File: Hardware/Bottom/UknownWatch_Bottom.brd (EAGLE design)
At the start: 33 x 33 mm, 31 parts, among them U1 AD5242-SO16

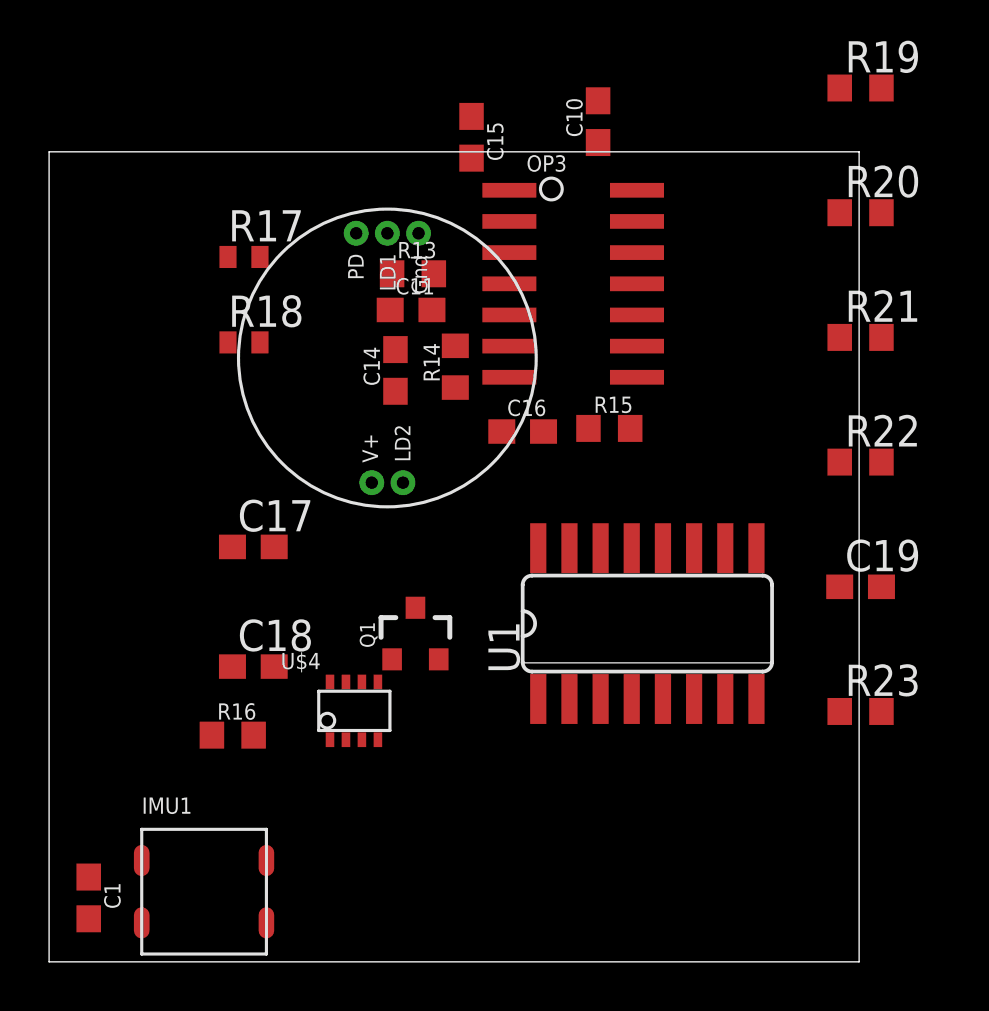
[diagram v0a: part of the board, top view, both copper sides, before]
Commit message: Added connections from bottom to top board and other various changes.
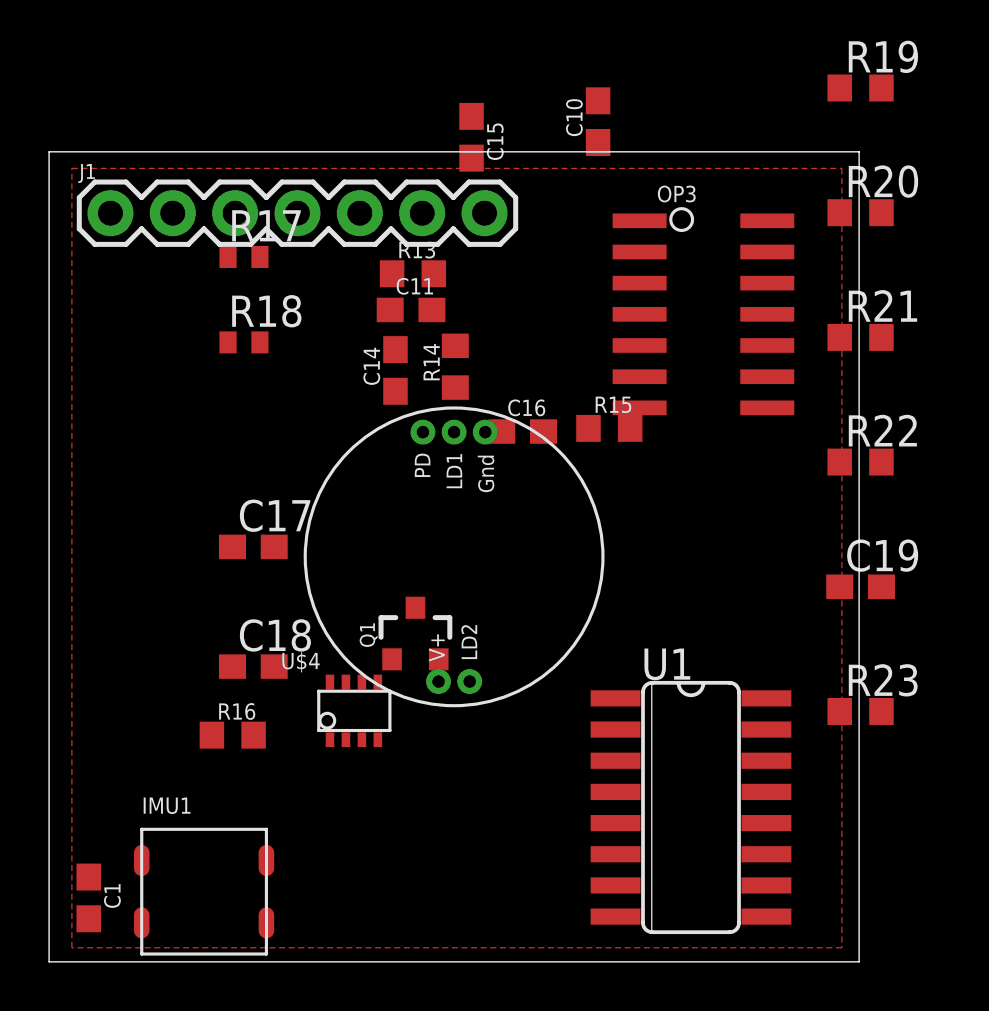
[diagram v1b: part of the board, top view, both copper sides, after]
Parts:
- added J1: (no value), LinnesLab-Connectors:1X07
- moved U$3 8.55 mm to (19.0, 19.0)
- moved U1 7.70 mm to (28.7, 8.79), turned to 270 degrees
- moved OP3 5.45 mm to (29.2, 28.9)
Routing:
- added copper zone on layer 1, net 3.3V

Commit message: Made all changes associated wih take 002
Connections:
- removed net LED.CTRL: U$4.8
- removed net TIA: C10.2, C15.1, OP4.1, U1.3
- new net A6/TIA: C10.2, C15.1, J1.5, OP4.1, U1.3
- new net A7/PPG: C21.2, J1.7, OP3.1
- new net D29/LED.CTRL: J1.6, U$4.8
- net PPG: no longer C21.2, OP3.1
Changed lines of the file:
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@@
 <wire x1="11.3538" y1="4.0894" x2="15.8946" y2="11.549" width="0" layer="19" extent="1-1"/>
 </signal>
-<signal name="TIA">
+<signal name="A6/TIA">
 <contactref element="C10" pad="2"/>
 <contactref element="U1" pad="3"/>
 <contactref element="C15" pad="1"/>
 <contactref element="OP4" pad="1"/>
+<contactref element="J1" pad="5"/>
 <wire x1="24.8666" y1="37.5784" x2="43.5" y2="31.714" width="0" layer="19" extent="1-1"/>
 <wire x1="19.7104" y1="36.9434" x2="24.8666" y2="37.5784" width="0" layer="19" extent="1-1"/>
-<wire x1="25.5778" y1="10.6934" x2="24.8666" y2="37.5784" width="0" layer="19" extent="1-1"/>
+<wire x1="15.16" y1="33" x2="19.7104" y2="36.9434" width="0" layer="19" extent="1-1"/>
+<wire x1="25.5778" y1="10.6934" x2="15.16" y2="33" width="0" layer="19" extent="1-1"/>
 </signal>
 <signal name="PD.C">
@@
 <wire x1="9.1322" y1="11.7348" x2="13.9446" y2="11.549" width="0" layer="19" extent="1-1"/>
 </signal>
-<signal name="LED.CTRL">
+<signal name="D29/LED.CTRL">
 <contactref element="U$4" pad="8"/>
+<contactref element="J1" pad="6"/>
+<wire x1="13.9446" y1="13.9018" x2="17.7" y2="33" width="0" layer="19" extent="1-1"/>
 </signal>
 <signal name="N$10">
@@
 <signal name="PPG">
 <contactref element="U1" pad="14"/>
-<contactref element="C21" pad="2"/>
-<contactref element="OP3" pad="1"/>
-<wire x1="31.7246" y1="10.6934" x2="44.03" y2="17.78" width="0" layer="19" extent="1-1"/>
-<wire x1="26.5592" y1="32.6898" x2="31.7246" y2="10.6934" width="0" layer="19" extent="1-1"/>
 </signal>
 <signal name="N$13">
@@
 <wire x1="44.03" y1="22.86" x2="44.03" y2="27.94" width="0" layer="19" extent="1-1"/>
 </signal>
+<signal name="A7/PPG">
+<contactref element="C21" pad="2"/>
+<contactref element="OP3" pad="1"/>
+<contactref element="J1" pad="7"/>
+<wire x1="26.5592" y1="32.6898" x2="44.03" y2="17.78" width="0" layer="19" extent="1-1"/>
+<wire x1="20.24" y1="33" x2="26.5592" y2="32.6898" width="0" layer="19" extent="1-1"/>
+</signal>
 </signals>

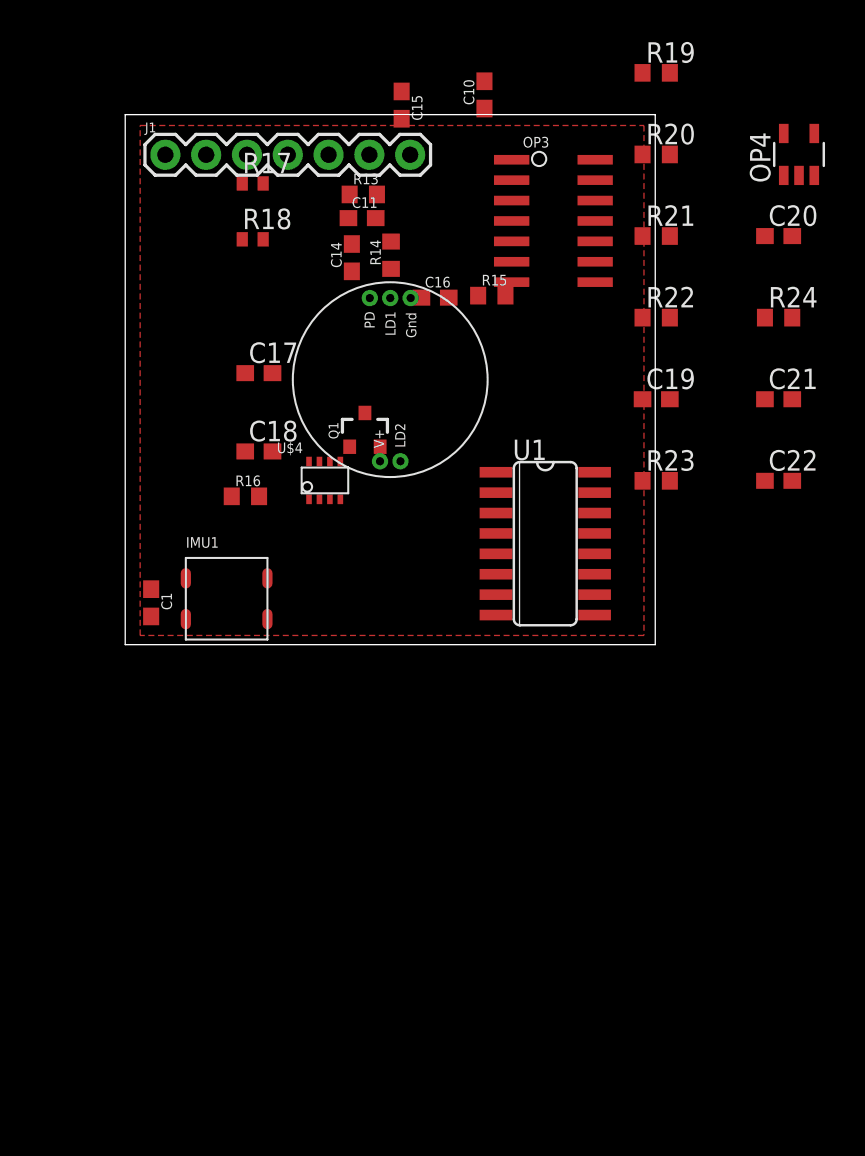
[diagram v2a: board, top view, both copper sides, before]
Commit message: Worked on routing for bottom board.
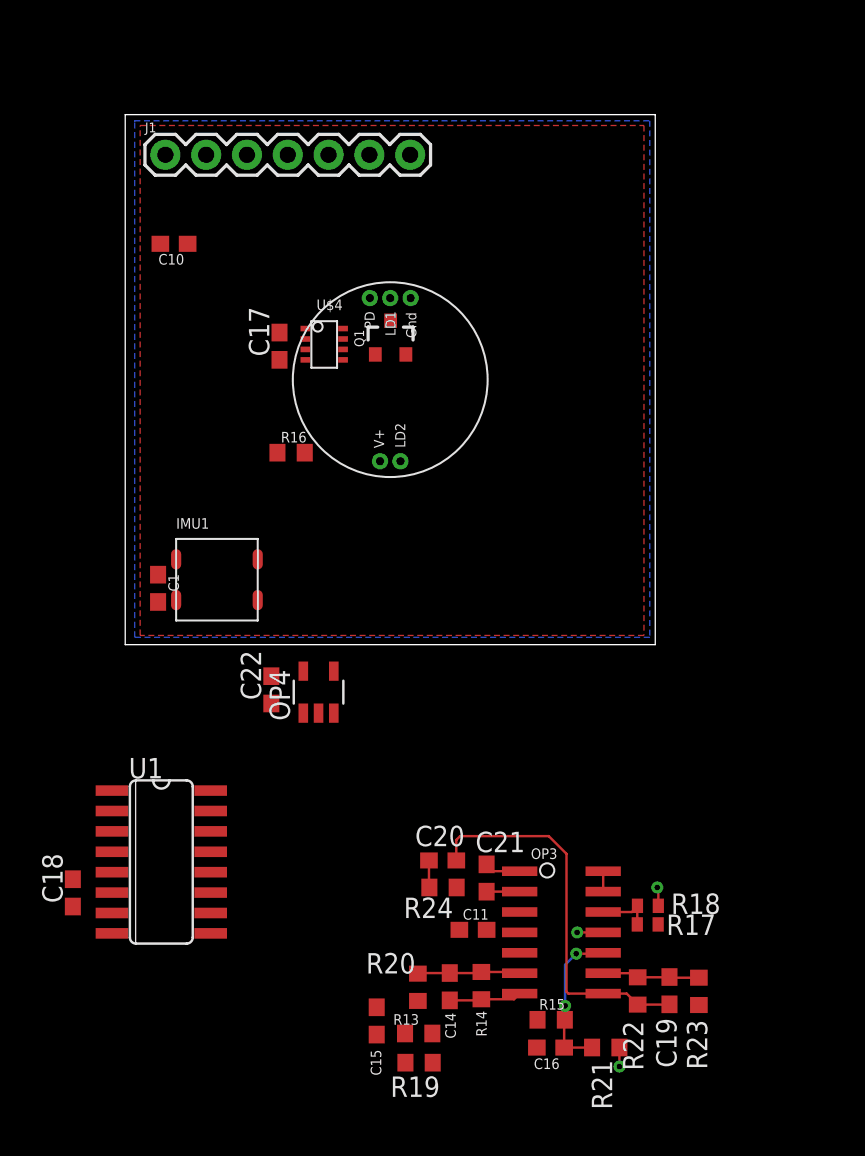
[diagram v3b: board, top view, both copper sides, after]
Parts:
- moved R19 63.4 mm to (20.8, -23.5), turned to 180 degrees
- moved C15 57.0 mm to (18.2, -20.9)
- moved R20 53.9 mm to (20.7, -18.8), turned to 90 degrees
- moved R13 52.4 mm to (20.8, -21.7)
- moved R17 52.3 mm to (35.0, -14.9)
- moved R21 50.6 mm to (32.4, -22.6), turned to 180 degrees
- moved R18 48.2 mm to (35.0, -13.8), turned to 180 degrees
- moved C16 47.2 mm to (29.0, -22.6)
- moved R14 45.8 mm to (24.7, -18.7), turned to 270 degrees
- moved C14 45.8 mm to (22.7, -18.8)
- moved R15 45.2 mm to (29.0, -20.9), turned to 180 degrees
- moved OP4 44.9 mm to (14.5, -0.46)
- moved C11 44.8 mm to (24.2, -15.3)
- moved OP3 44.3 mm to (29.7, -15.4)
- moved C20 44.1 mm to (22.3, -10.9), turned to 180 degrees
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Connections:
- removed net LED: Q1.3
- net LED.C: now also Q1.3
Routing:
- net N$19: track 0.00 -> 24.2 mm
- net N$17: track 0.00 -> 8.79 mm, vias 0 -> 2
- net N$15: track 0.00 -> 6.84 mm
- net N$18: track 0.00 -> 6.09 mm
- net N$16: track 0.00 -> 4.60 mm
- net GND: track 0.00 -> 3.98 mm, vias 0 -> 3
- net N$10: track 0.00 -> 3.42 mm
- net A7/PPG: track 0.00 -> 2.23 mm
- net G.W2: track 0.00 -> 2.06 mm
- net N$20: track 0.00 -> 1.69 mm
- net VREF: track 0.00 -> 1.27 mm
- added copper zone on layer 16, net GND

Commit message: Made associated changes up to 41:07 in take 003.
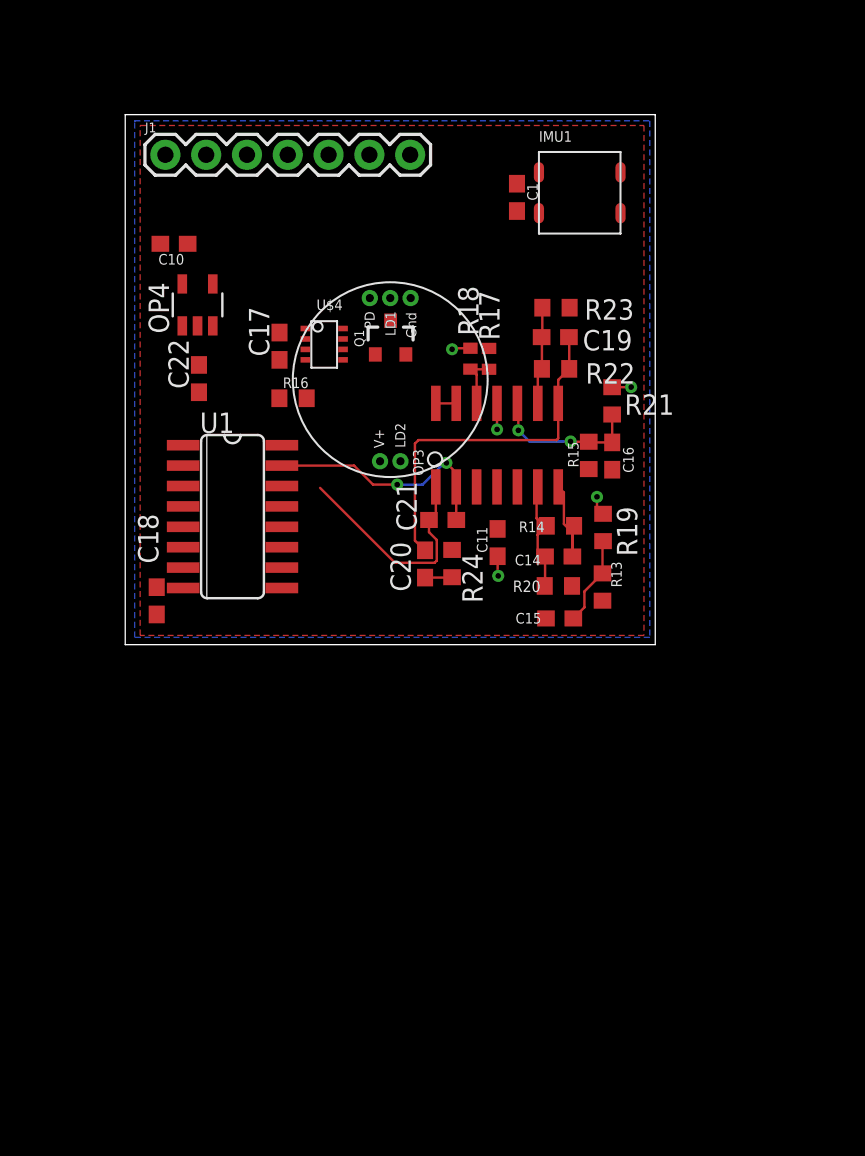
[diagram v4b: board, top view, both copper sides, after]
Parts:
- moved R23 43.5 mm to (29.3, 23.5), turned to 180 degrees
- moved C19 41.3 mm to (29.3, 21.6), turned to 180 degrees
- moved R21 40.3 mm to (32.8, 17.7), turned to 270 degrees
- moved R22 39.1 mm to (29.3, 19.7), turned to 0 degrees
- moved C16 37.0 mm to (32.8, 14.2), turned to 90 degrees
- moved R17 36.6 mm to (25.2, 20.3), turned to 90 degrees
- moved R18 35.8 mm to (24.0, 20.3), turned to 270 degrees
- moved R19 35.2 mm to (32.3, 9.80), turned to 270 degrees
- moved R15 35.2 mm to (31.4, 14.3), turned to 270 degrees
- moved C1 33.0 mm to (26.9, 30.3)
- moved IMU1 33.0 mm to (30.8, 30.6)
- moved OP3 30.6 mm to (25.6, 14.9), turned to 0 degrees
- moved R13 30.1 mm to (32.2, 6.09), turned to 270 degrees
- moved R14 29.0 mm to (29.6, 9.90), turned to 0 degrees
- moved C14 27.6 mm to (29.5, 7.99), turned to 180 degrees
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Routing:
- net G.W2: track 2.06 -> 14.3 mm, vias 0 -> 2
- net A7/PPG: track 2.23 -> 14.2 mm
- net N$13: track 0.00 -> 5.58 mm
- net GND: track 3.98 -> 6.43 mm, vias 3 -> 5
- net N$16: track 4.60 -> 6.65 mm
- net N$19: track 24.2 -> 22.8 mm
- net N$15: track 6.84 -> 7.41 mm

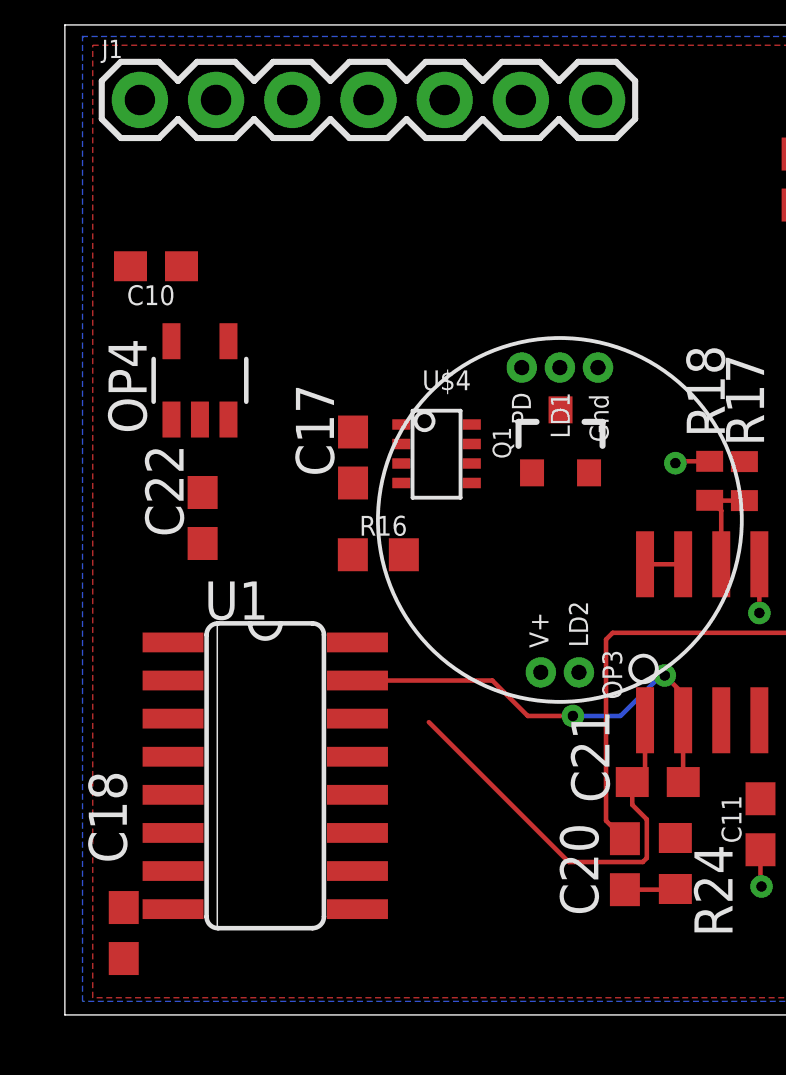
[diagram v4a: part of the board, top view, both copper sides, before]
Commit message: Routed more of the bottom board
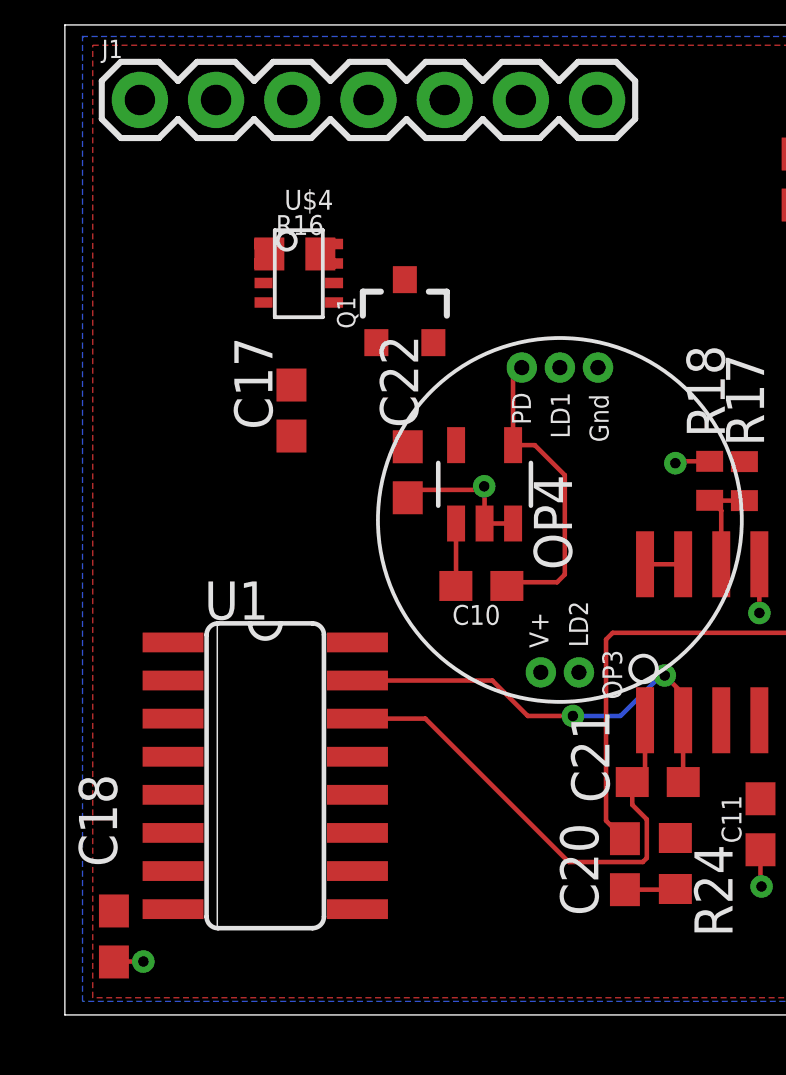
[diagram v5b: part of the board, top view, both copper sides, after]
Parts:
- moved C10 15.2 mm to (16.4, 16.8)
- moved R16 10.4 mm to (10.2, 27.9)
- moved OP4 10.1 mm to (16.5, 20.2)
- moved U$4 7.57 mm to (10.3, 27.2)
- moved C22 7.01 mm to (13.9, 20.6)
- moved Q1 6.77 mm to (13.8, 25.9)
- moved C17 2.58 mm to (10.1, 22.6)
- moved C18 0.35 mm to (4.14, 5.12)
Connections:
- removed net PPG: U1.14
- net A7/PPG: now also U1.14
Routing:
- net PD.C: track 0.00 -> 10.2 mm
- net GND: track 6.43 -> 12.3 mm, vias 5 -> 7
- net A7/PPG: track 14.2 -> 16.6 mm
- net A6/TIA: track 0.00 -> 2.09 mm

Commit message: Worked on routing of bottom board
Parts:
- J1: device LinnesLab-Connectors:1X07 -> LinnesLab-Connectors:1X07_1.27MM
- moved IMU1 24.5 mm to (6.39, 28.7), turned to 90 degrees
- moved C1 23.3 mm to (4.83, 22.8)
- moved U$4 9.69 mm to (11.7, 17.6)
- moved R16 8.54 mm to (8.51, 19.5), turned to 90 degrees
- moved C18 5.47 mm to (5.31, 10.5), turned to 270 degrees
- moved Q1 5.18 mm to (18.9, 26.8), turned to 180 degrees
- moved C17 3.20 mm to (6.86, 22.8), turned to 270 degrees
- moved U1 1.48 mm to (10.6, 10.7)
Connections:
- net 3.3V: now also J1.4
- net GND: now also J1.3
- net SCL: now also J1.2
- net SDA: now also J1.1
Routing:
- net A6/TIA: track 2.09 -> 35.3 mm, vias 0 -> 2
- net PD.C: track 10.2 -> 24.8 mm, vias 0 -> 2
- net GND: track 12.3 -> 24.0 mm, vias 7 -> 10
- net SCL: track 0.00 -> 2.60 mm
- net SDA: track 0.00 -> 1.82 mm
- net LED.C: track 0.00 -> 1.69 mm
- net G.W2: track 14.3 -> 12.9 mm
- net A7/PPG: track 16.6 -> 15.9 mm
